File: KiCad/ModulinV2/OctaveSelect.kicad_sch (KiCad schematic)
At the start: 37 parts, among them IC18 SN74LV10ADR, IC19 SN74LV10ADR, IC20 SN74LV10ADR, IC21 SN74HC193DR, IC22 TMUX4051DYYRQ1, IC23 TL072HIDR, SW2 Rocker Switch

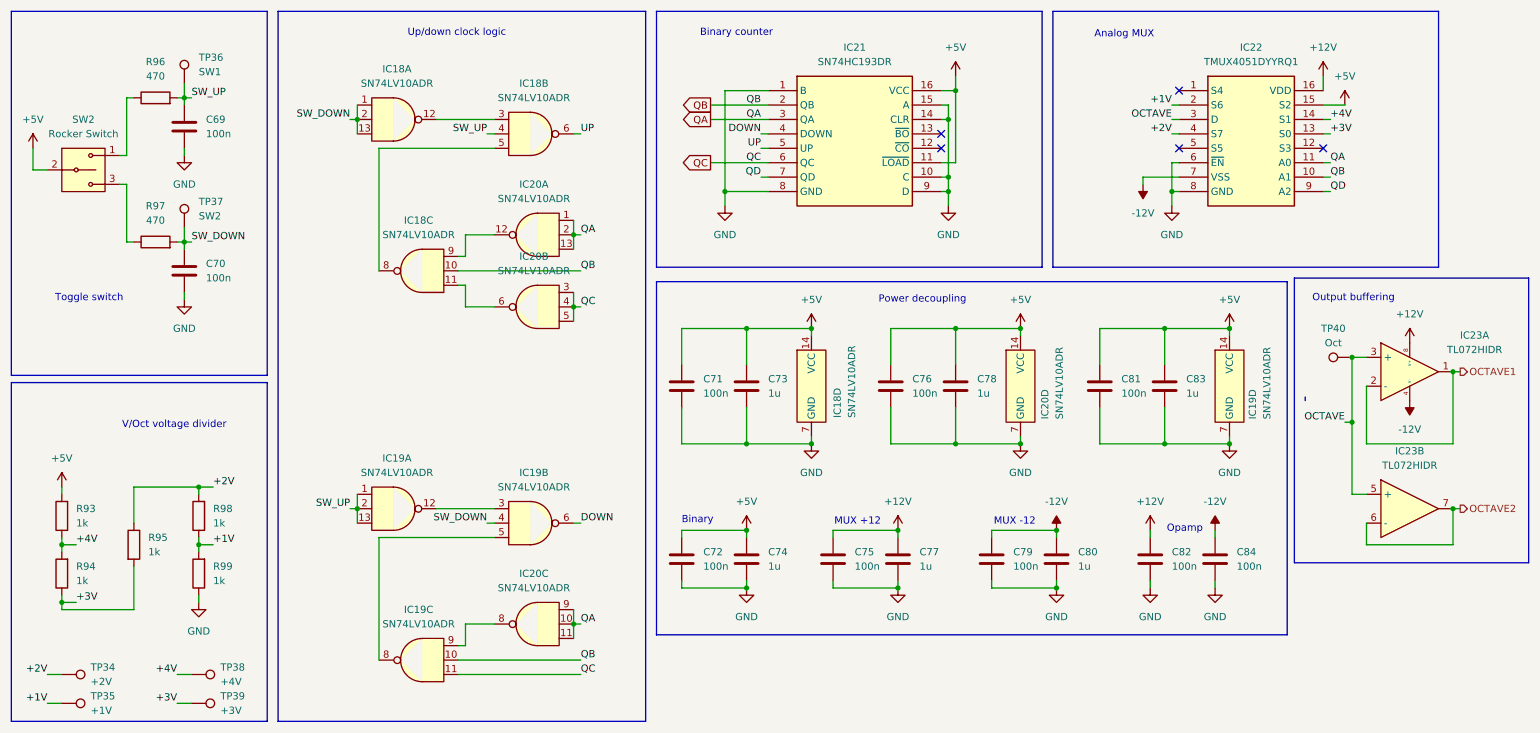
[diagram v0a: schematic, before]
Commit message: Completed tuning & mod wheel layouts
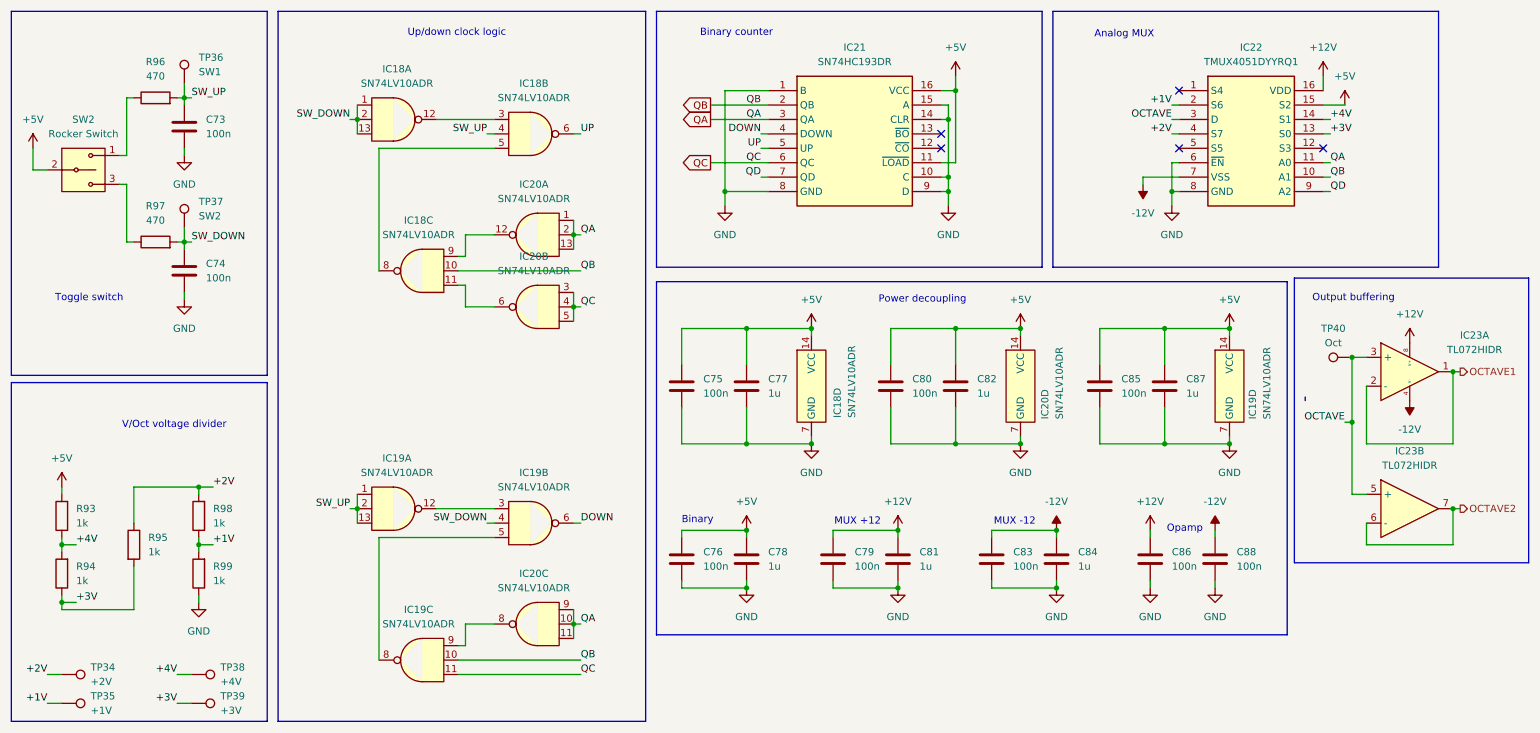
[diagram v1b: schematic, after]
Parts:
- renumbered C69 to C73, C70 to C74, C71 to C75, C72 to C76, C73 to C77, C74 to C78, C75 to C79, C76 to C80, C77 to C81, C78 to C82, C79 to C83, C80 to C84, C81 to C85, C82 to C86, C83 to C87, C84 to C88

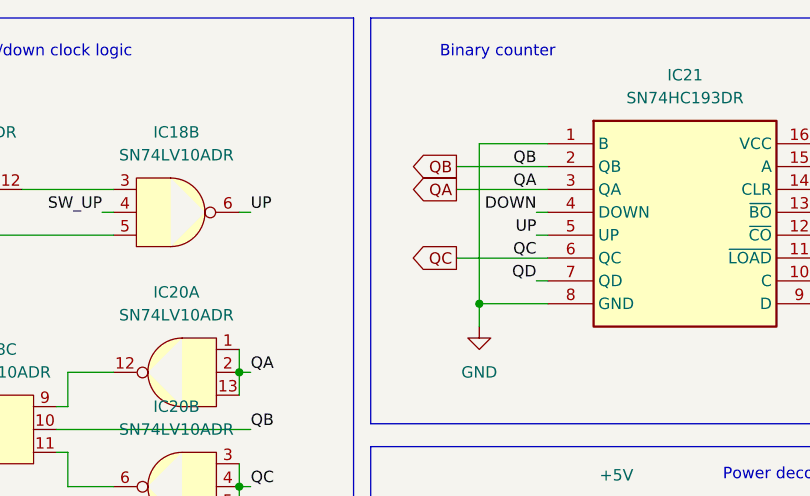
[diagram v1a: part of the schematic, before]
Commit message: FInished LFO, octave/wave selector and UI layout
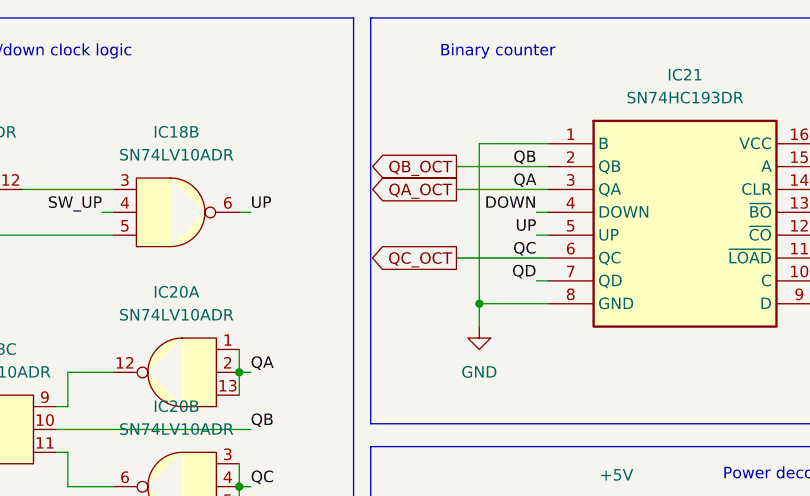
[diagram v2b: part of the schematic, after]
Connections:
- net QA renamed QA_OCT
- net QB renamed QB_OCT
- net QC renamed QC_OCT
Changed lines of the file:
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@@
 		)
 	)
-	(global_label "QA"
+	(global_label "QA_OCT"
 		(shape output)
 		(at 138.43 53.34 180)
@@
 		)
 		(property "Intersheetrefs" "${INTERSHEET_REFS}"
-			(at 133.0257 53.34 0)
+			(at 128.49 53.34 0)
 			(effects
 				(font
@@
 		)
 	)
-	(global_label "QB"
+	(global_label "QB_OCT"
 		(shape output)
 		(at 138.43 50.8 180)
@@
 		)
 		(property "Intersheetrefs" "${INTERSHEET_REFS}"
-			(at 132.8443 50.8 0)
+			(at 128.3086 50.8 0)
 			(effects
 				(font
@@
 		)
 	)
-	(global_label "QC"
+	(global_label "QC_OCT"
 		(shape output)
 		(at 138.43 60.96 180)
@@
 		)
 		(property "Intersheetrefs" "${INTERSHEET_REFS}"
-			(at 132.8443 60.96 0)
+			(at 128.3086 60.96 0)
 			(effects
 				(font

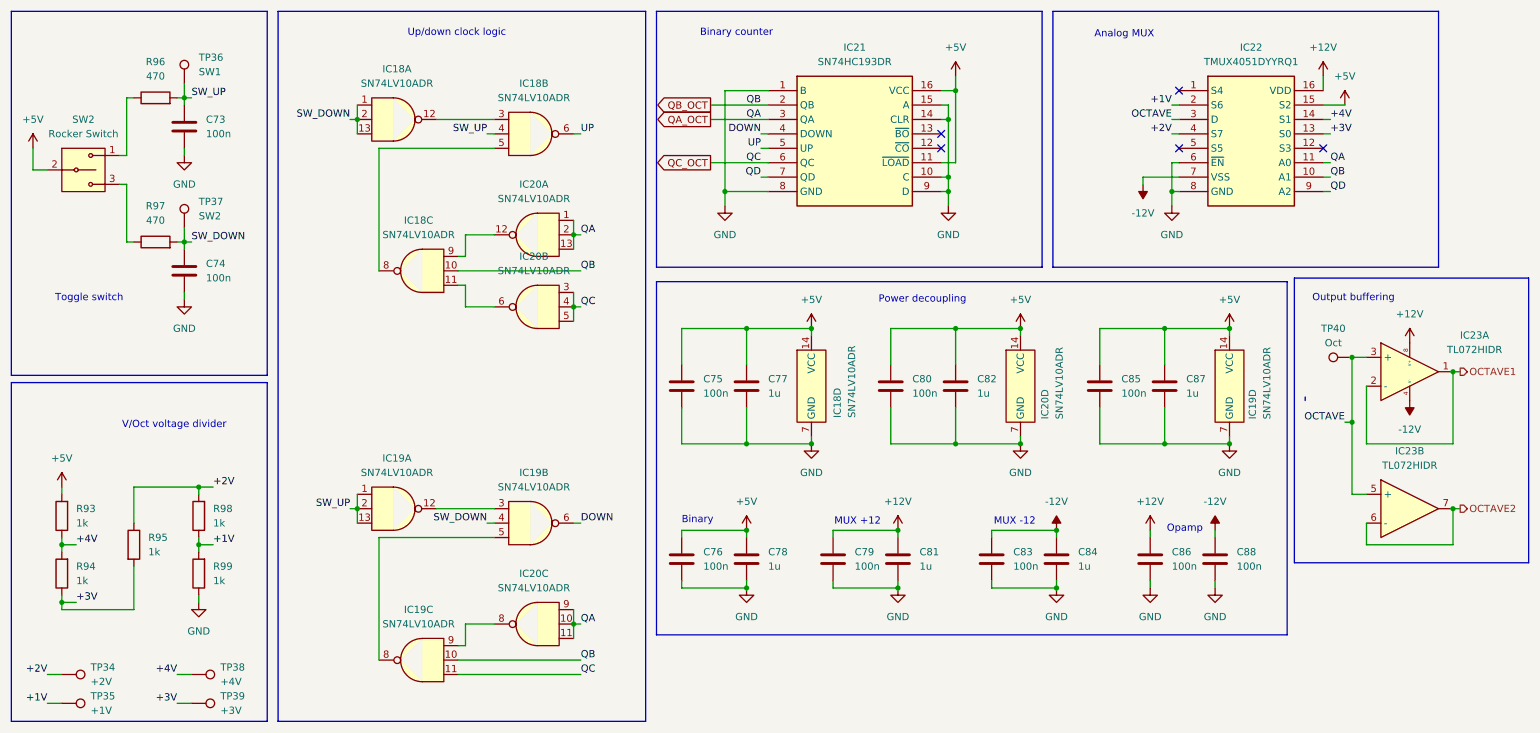
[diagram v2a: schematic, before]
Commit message: Fixed schematic connections
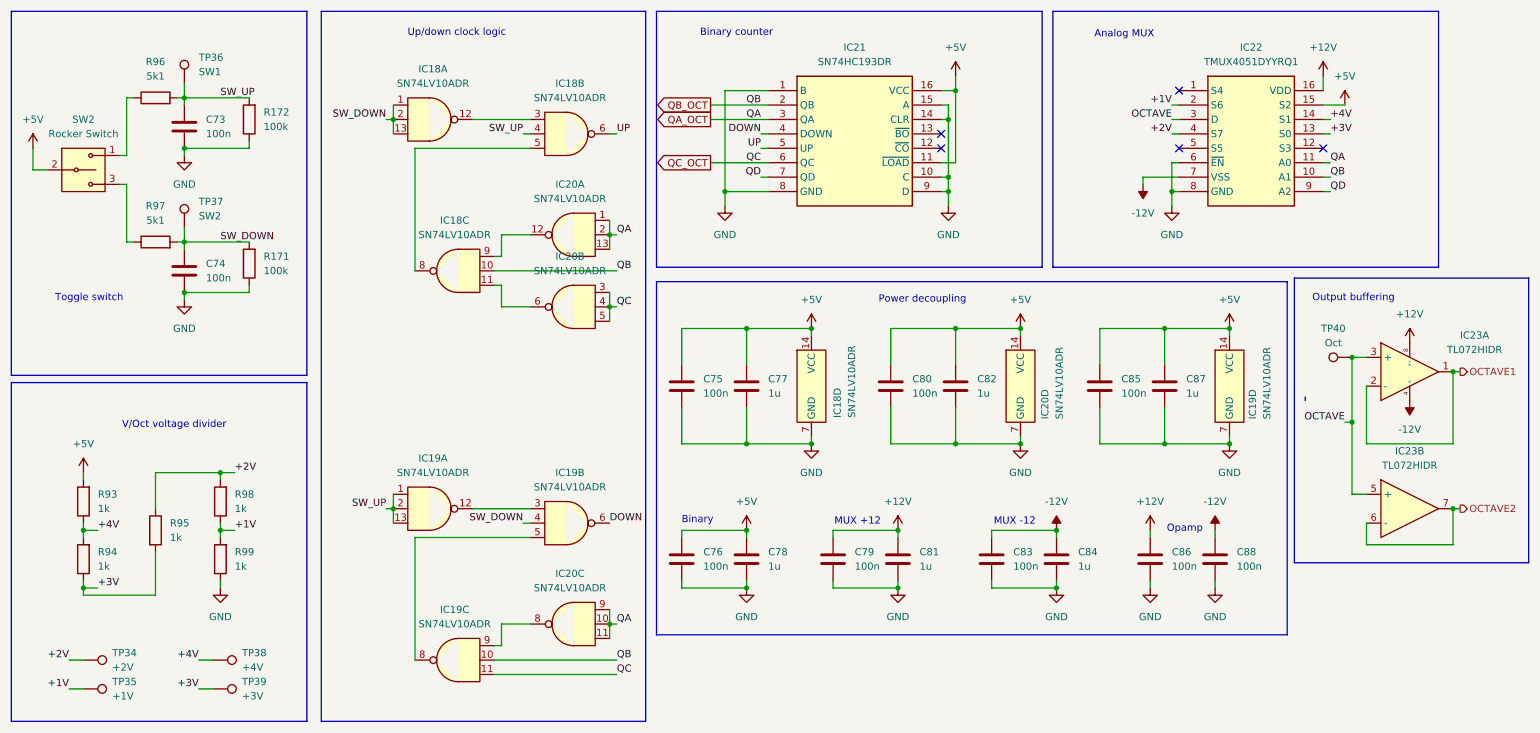
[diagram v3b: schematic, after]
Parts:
- added R171, R172: 100k, Resistor_SMD:R_0603_1608Metric_Pad0.98x0.95mm_HandSolder, symbol Device:R
- R96, R97: value 470 -> 5k1
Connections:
- net GND: now also R171.1, R172.1
- net SW_DOWN: now also R171.2
- net SW_UP: now also R172.2
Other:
- company: (none) -> TalTech
- moved on the sheet: IC18A, IC18B, IC18C, IC19A, IC19B, IC19C, IC20A, IC20B, IC20C, R93, R94, R95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
